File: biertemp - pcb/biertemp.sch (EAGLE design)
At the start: 32 parts, among them IC1 MEGA8-P, K1 G5LE, Q1 12MHz, Q2 32,768kHz

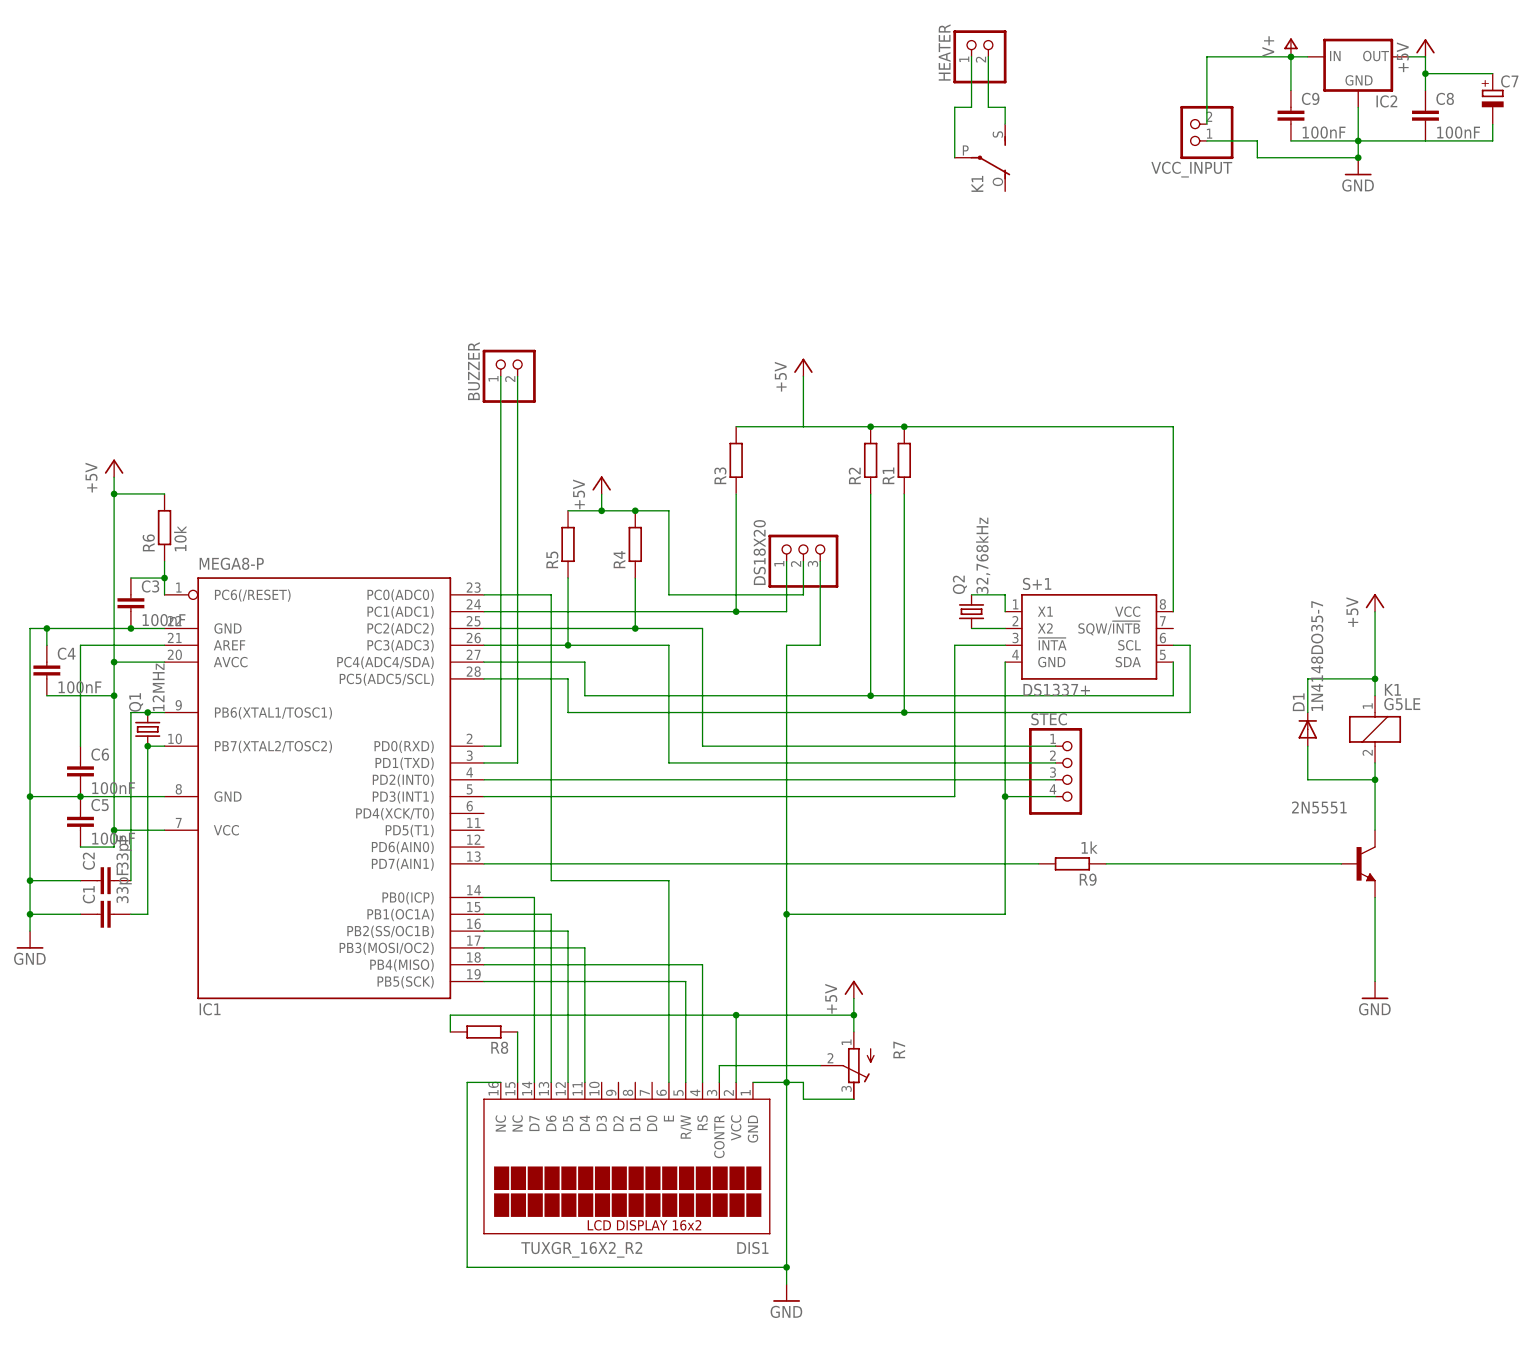
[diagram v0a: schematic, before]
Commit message: first pcb version finished, including pcb design changed ports for better layout NEW: All port definitions now with macros
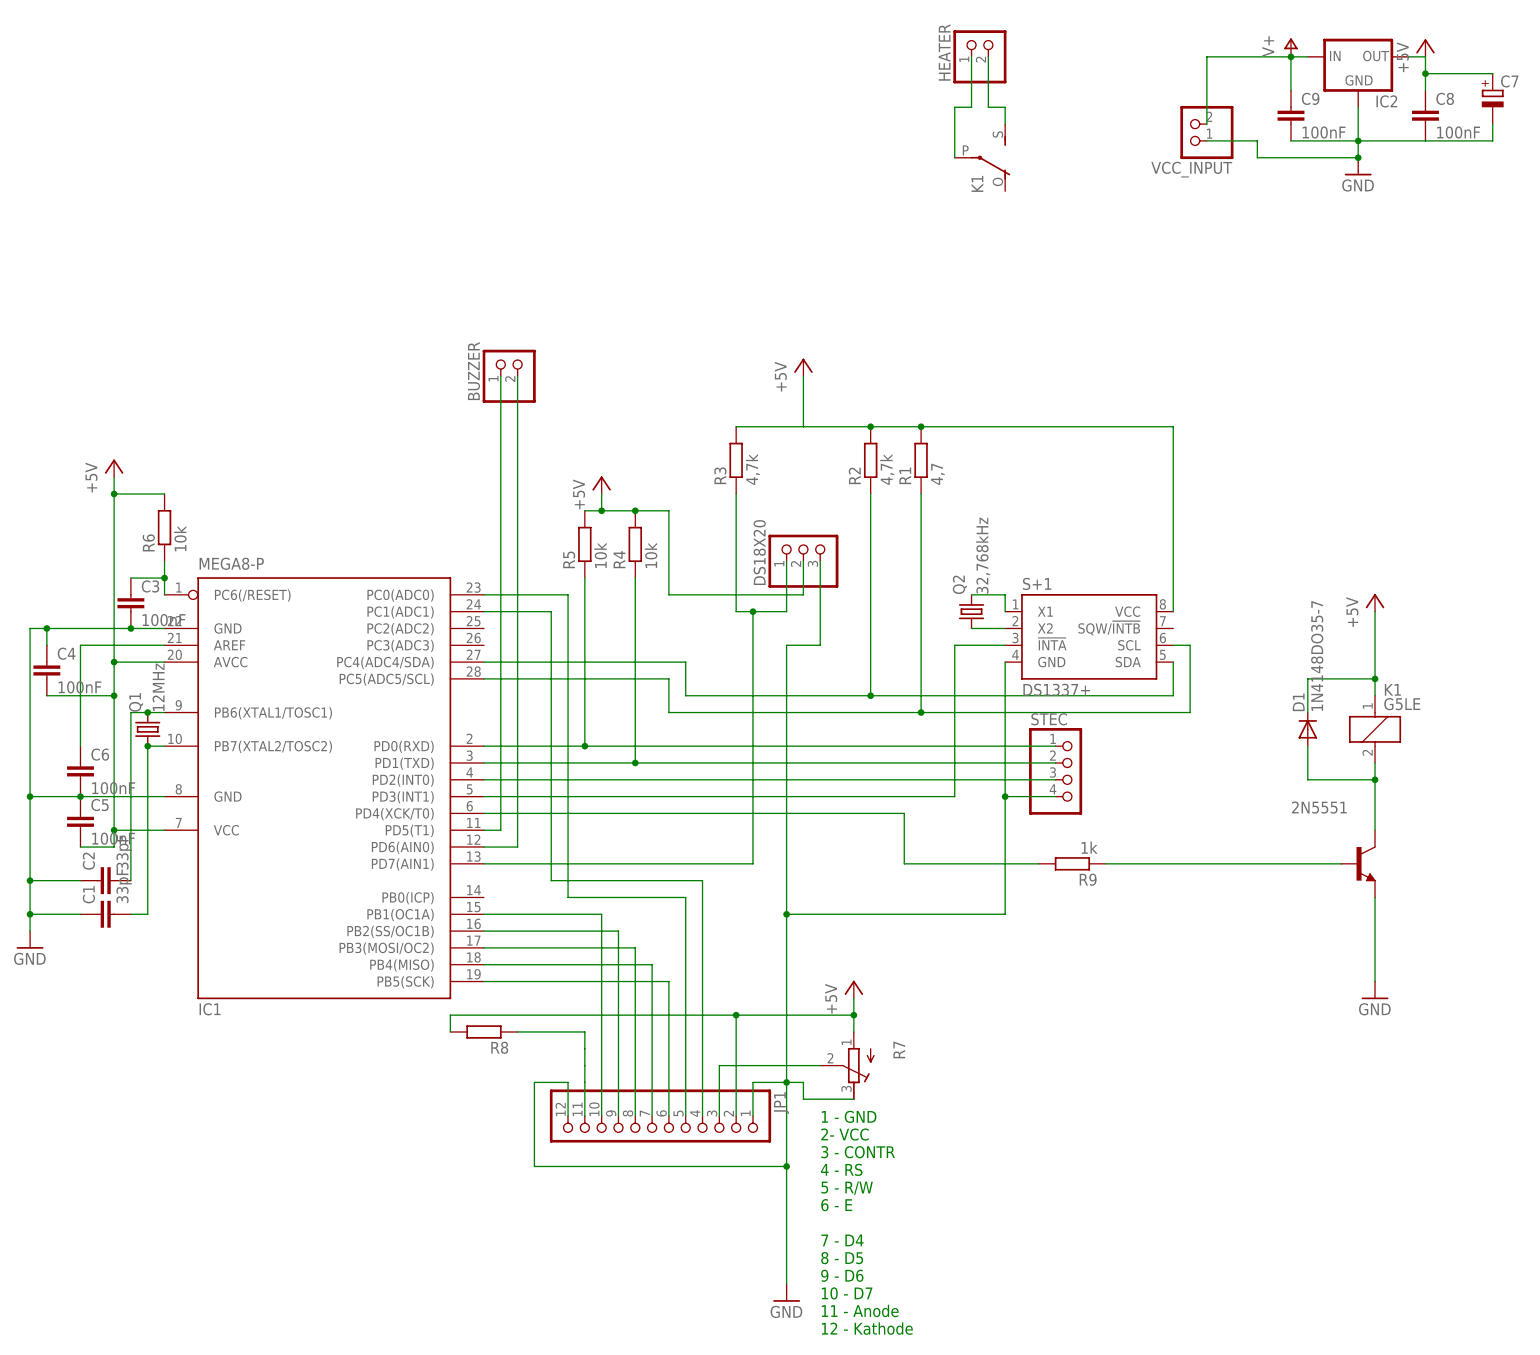
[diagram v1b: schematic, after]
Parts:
- removed DIS1: TUXGR_16X2_R2, display-lcd:TUXGR_16X2_R2
- added JP1: (no value), pinhead:PINHD-1X12
- R1: value (none) -> 4,7
- R2, R3: value (none) -> 4,7k
- R4, R5: value (none) -> 10k
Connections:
- net +5V: now also JP1.2; no longer DIS1.VCC
- net GND: now also JP1.1, JP1.12; no longer DIS1.GND, DIS1.NC@2
- net N$14: now also IC1.PB1(OC1A), JP1.10; no longer DIS1.D7, IC1.PB0(ICP)
- net N$15: now also JP1.11; no longer DIS1.NC@1
- net N$16: now also JP1.3; no longer DIS1.CONTR
- net N$17: now also IC1.PB2(SS/OC1B), JP1.9; no longer DIS1.RS, IC1.PB4(MISO)
- net N$18: now also IC1.PB3(MOSI/OC2), JP1.8; no longer DIS1.R/W, IC1.PB5(SCK)
- net N$19: now also IC1.PB4(MISO), JP1.7; no longer DIS1.E, IC1.PC0(ADC0)
- net N$2: now also IC1.PD7(AIN1); no longer IC1.PC1(ADC1)
- net N$20: now also IC1.PB5(SCK), JP1.6; no longer DIS1.D4, IC1.PB3(MOSI/OC2)
- net N$21: now also IC1.PC0(ADC0), JP1.5; no longer DIS1.D5, IC1.PB2(SS/OC1B)
- net N$22: now also IC1.PC1(ADC1), JP1.4; no longer DIS1.D6, IC1.PB1(OC1A)
- net N$24: now also IC1.PD5(T1); no longer IC1.PD0(RXD)
- net N$25: now also IC1.PD0(RXD), R5.1, STEC.1; no longer BUZZER.2, IC1.PD1(TXD)
- net N$26: now also BUZZER.2, IC1.PD6(AIN0); no longer IC1.PD7(AIN1), R9.2
- net N$8: now also IC1.PD4(XCK/T0), R9.2; no longer IC1.PC2(ADC2), R4.1, STEC.1
- net N$9: now also IC1.PD1(TXD), R4.1; no longer IC1.PC3(ADC3), R5.1
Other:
- note added: "1 - GND 2- VCC 3 - CONTR 4 - RS 5 - R/W 6 - E 7 - D4 8 - D5 9 - D6 10 - D7 11 - Anode 12 - Kathode"
- moved on the sheet: R1, R5
